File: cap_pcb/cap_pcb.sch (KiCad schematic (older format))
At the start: 43 parts, among them U0 ATtiny85-20PU, U1 PCF8574, U10 HDSP-7803, U11 HDSP-7803, U12 PCF8574, U2 HDSP-7803, U3 PCF8574, U4 HDSP-7803, U5 PCF8574, U6 HDSP-7803, U7 PCF8574, U8 HDSP-7803, U9 PCF8574

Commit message: mostly finished pcb
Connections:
- net at R1.2, U0.5 (AREF/PB0), U1.14 (SCL)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: no longer U5.15 (SDA)
- net at R0.2, U0.7 (PB2), U1.15 (SDA)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: now also U5.15 (SDA)
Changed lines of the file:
@@
 Wire Wire Line
 	4650 3250 4100 3250
-Wire Wire Line
-	4100 3250 4100 2750
 Connection ~ 4100 1250
 Wire Wire Line
@@
 	4650 3350 4250 3350
 Wire Wire Line
-	4250 3350 4250 2650
+	4250 3350 4250 2750
 Connection ~ 4250 1350
 Wire Wire Line
@@
 	1100 3400 1200 3400
 Wire Wire Line
-	4100 2750 900  2750
-Wire Wire Line
 	900  2750 900  3500
 Wire Wire Line
 	900  3500 1200 3500
-Connection ~ 4100 2750
-Wire Wire Line
-	4100 2750 4100 2600
 Wire Wire Line
 	9300 1200 9600 1200
@@
 Wire Wire Line
 	2000 6850 2000 7050
+Wire Wire Line
+	4100 2600 4100 3250
+Wire Wire Line
+	900  2750 4250 2750
+Connection ~ 4250 2750
+Wire Wire Line
+	4250 2750 4250 2650
 $EndSCHEMATC

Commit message: finalized pcb, added source folder
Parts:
- added R14: 10k, Resistor_THT:R_Axial_DIN0411_L9.9mm_D3.6mm_P25.40mm_Horizontal, symbol Device:R
- added SW1: SW_MEC_5E, Button_Switch_THT:SW_MEC_5GTH9, symbol Switch:SW_MEC_5E
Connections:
- net GND: now also R14.2
- net VCC: now also SW1.4 (A)
- net at U0.3 (XTAL2/PB4): now also SW1.1
- new net: R14.1, SW1.2
- no-connect marks 1 -> 2
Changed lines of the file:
@@
 Wire Wire Line
 	4250 2750 4250 2650
+$Comp
+L Switch:SW_MEC_5E SW1
+U 1 1 5FA2A652
+P 3000 2050
+F 0 "SW1" H 3000 2435 50  0000 C CNN
+F 1 "SW_MEC_5E" H 3000 2344 50  0000 C CNN
+F 2 "Button_Switch_THT:SW_MEC_5GTH9" H 3000 2350 50  0001 C CNN
+F 3 "http://www.apem.com/int/index.php?controller=attachment&id_attachment=1371" H 3000 2350 50  0001 C CNN
+	1    3000 2050
+	1    0    0    -1
+$EndComp
+Wire Wire Line
+	2800 1950 2500 1950
+Wire Wire Line
+	2500 1950 2500 1650
+Wire Wire Line
+	2500 1650 2250 1650
+$Comp
+L Device:R R14
+U 1 1 5FA3D2A3
+P 2800 2200
+F 0 "R14" H 2870 2246 50  0000 L CNN
+F 1 "10k" H 2870 2155 50  0000 L CNN
+F 2 "Resistor_THT:R_Axial_DIN0411_L9.9mm_D3.6mm_P25.40mm_Horizontal" V 2730 2200 50  0001 C CNN
+F 3 "~" H 2800 2200 50  0001 C CNN
+	1    2800 2200
+	1    0    0    -1
+$EndComp
+$Comp
+L power:GND #PWR0101
+U 1 1 5FA69FA4
+P 2800 2350
+F 0 "#PWR0101" H 2800 2100 50  0001 C CNN
+F 1 "GND" H 2805 2177 50  0000 C CNN
+F 2 "" H 2800 2350 50  0001 C CNN
+F 3 "" H 2800 2350 50  0001 C CNN
+	1    2800 2350
+	1    0    0    -1
+$EndComp
+$Comp
+L power:VCC #PWR0102
+U 1 1 5FA6BB1A
+P 3400 1950
+F 0 "#PWR0102" H 3400 1800 50  0001 C CNN
+F 1 "VCC" H 3415 2123 50  0000 C CNN
+F 2 "" H 3400 1950 50  0001 C CNN
+F 3 "" H 3400 1950 50  0001 C CNN
+	1    3400 1950
+	1    0    0    -1
+$EndComp
+Wire Wire Line
+	3400 1950 3200 1950
+NoConn ~ 3200 2050
 $EndSCHEMATC

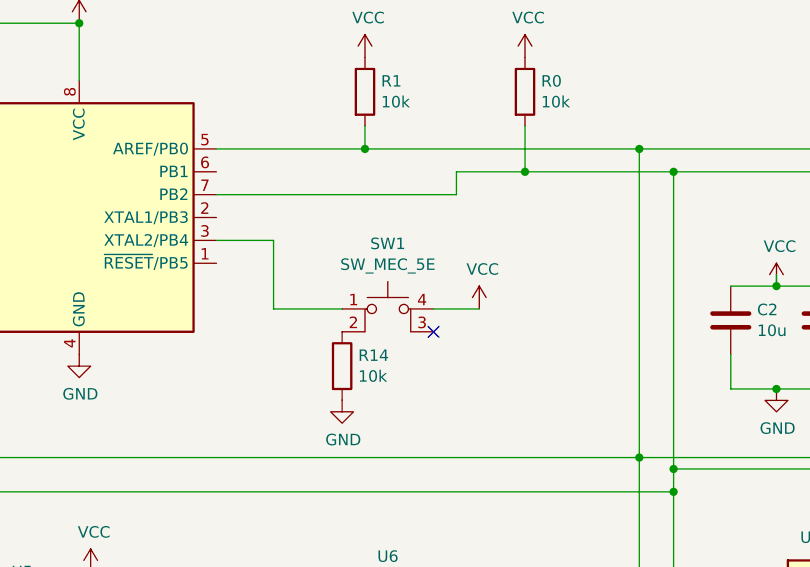
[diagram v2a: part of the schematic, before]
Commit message: fixed pcb to include proper ground (lol); added some src files for the attiny85
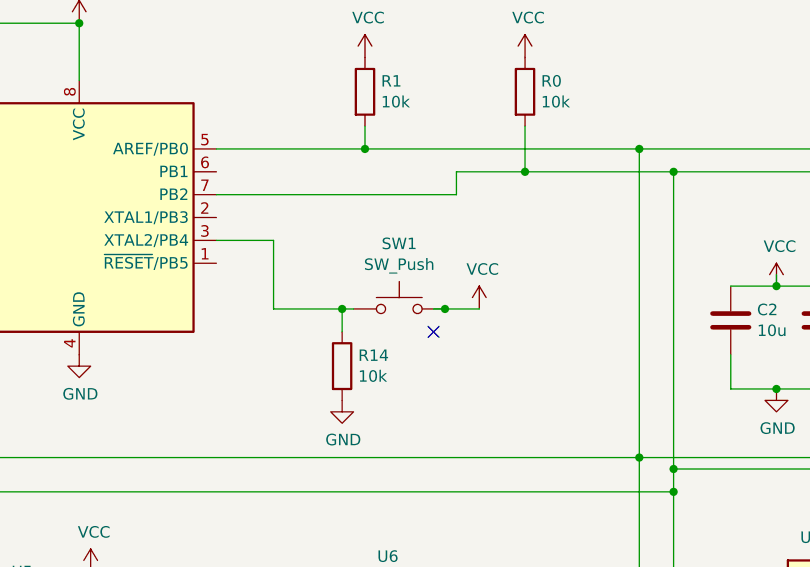
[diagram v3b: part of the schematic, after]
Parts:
- removed SW1: SW_MEC_5E, Button_Switch_THT:SW_MEC_5GTH9, symbol Switch:SW_MEC_5E
- added SW1: SW_Push, Button_Switch_THT:SW_PUSH_6mm, symbol Switch:SW_Push
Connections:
- net VCC: now also SW1.2
- net at U0.3 (XTAL2/PB4): now also R14.1, SW1.1
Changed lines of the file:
@@
 Wire Wire Line
 	4250 2750 4250 2650
-$Comp
-L Switch:SW_MEC_5E SW1
-U 1 1 5FA2A652
-P 3000 2050
-F 0 "SW1" H 3000 2435 50  0000 C CNN
-F 1 "SW_MEC_5E" H 3000 2344 50  0000 C CNN
-F 2 "Button_Switch_THT:SW_MEC_5GTH9" H 3000 2350 50  0001 C CNN
-F 3 "http://www.apem.com/int/index.php?controller=attachment&id_attachment=1371" H 3000 2350 50  0001 C CNN
-	1    3000 2050
-	1    0    0    -1
-$EndComp
 Wire Wire Line
 	2800 1950 2500 1950
@@
 $EndComp
 Wire Wire Line
-	3400 1950 3200 1950
+	3400 1950 3250 1950
 NoConn ~ 3200 2050
+$Comp
+L Switch:SW_Push SW1
+U 1 1 5FB4091C
+P 3050 1950
+F 0 "SW1" H 3050 2235 50  0000 C CNN
+F 1 "SW_Push" H 3050 2144 50  0000 C CNN
+F 2 "Button_Switch_THT:SW_PUSH_6mm" H 3050 2150 50  0001 C CNN
+F 3 "~" H 3050 2150 50  0001 C CNN
+	1    3050 1950
+	1    0    0    -1
+$EndComp
+Connection ~ 3250 1950
+Wire Wire Line
+	3250 1950 3200 1950
+Wire Wire Line
+	2800 2050 2800 1950
+Wire Wire Line
+	2850 1950 2800 1950
+Connection ~ 2800 1950
 $EndSCHEMATC
